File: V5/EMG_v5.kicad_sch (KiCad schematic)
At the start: 20 parts, among them J1 SJ1-3523N, J2 Output, U1 INA333xxDGK, U2 MCP6002-xP

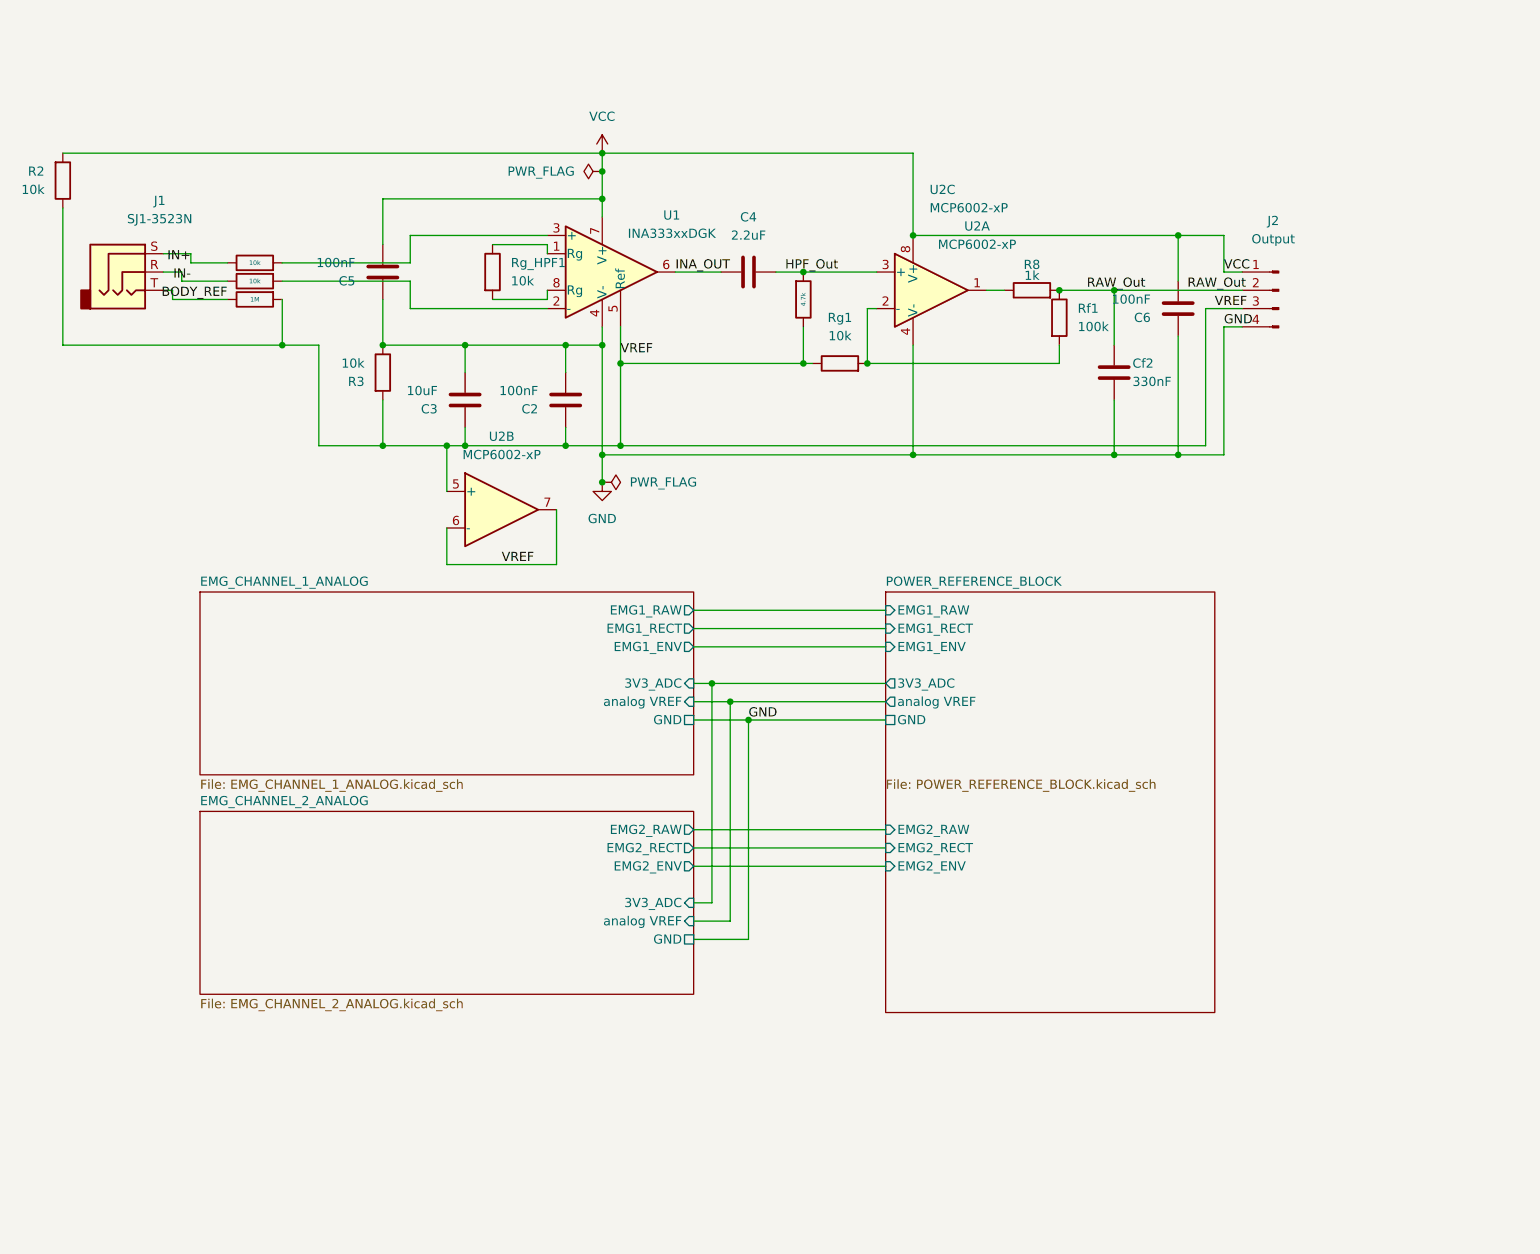
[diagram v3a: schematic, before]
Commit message: remove legacy root emg schematic block
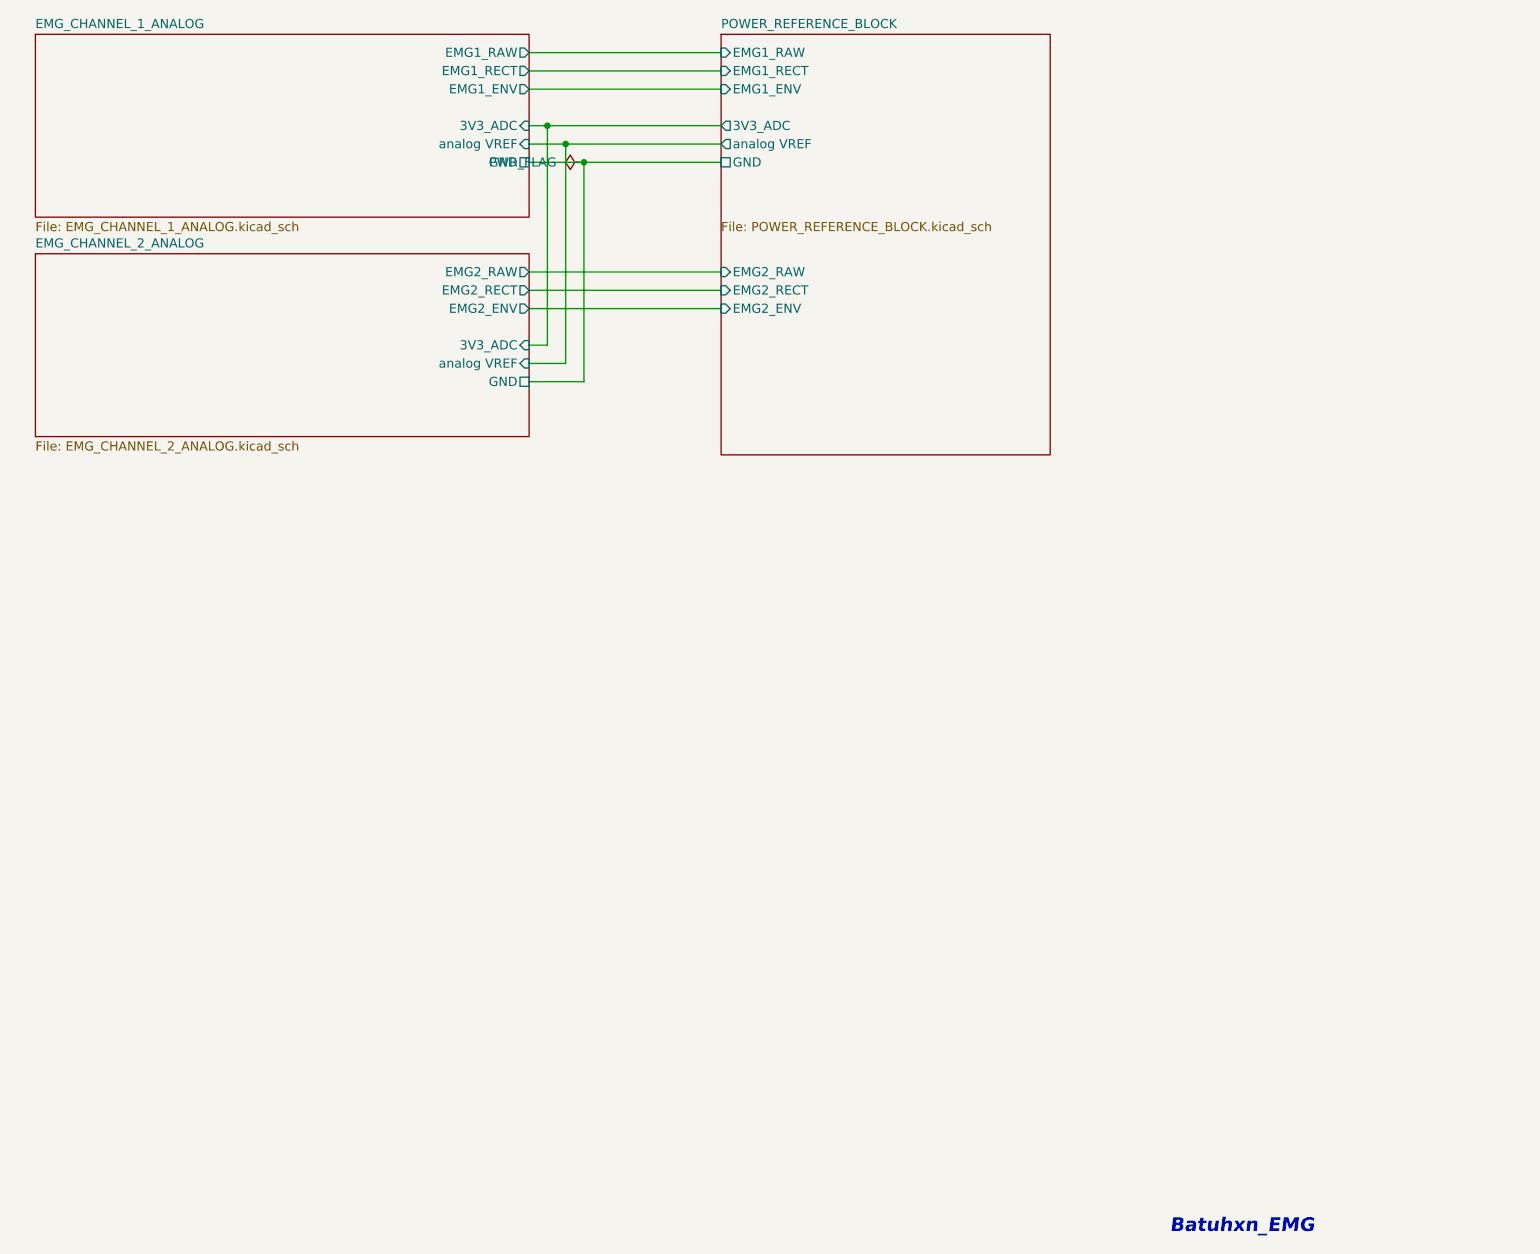
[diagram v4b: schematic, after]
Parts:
- removed C2, C5, C6: 100nF, Capacitor_THT:C_Disc_D5.0mm_W2.5mm_P5.00mm, symbol Device:C
- removed C3: 10uF, Capacitor_THT:CP_Radial_D5.0mm_P2.50mm, symbol Device:C
- removed C4: 2.2uF, Capacitor_THT:C_Disc_D5.0mm_W2.5mm_P5.00mm, symbol Device:C
- removed Cf2: 330nF, Capacitor_THT:C_Disc_D5.0mm_W2.5mm_P5.00mm, symbol Device:C
- removed J1: SJ1-3523N, Connector_Audio:Jack_3.5mm_CUI_SJ1-3523N_Horizontal, symbol Connector_Audio:AudioJack3
- removed J2: Output, Connector_PinHeader_2.54mm:PinHeader_1x04_P2.54mm_Vertical, symbol Connector:Conn_01x04_Pin
- removed R2, R3, R4, R5, Rg1, Rg_HPF1: 10k, Resistor_THT:R_Axial_DIN0207_L6.3mm_D2.5mm_P7.62mm_Horizontal, symbol Device:R
- removed R6: 4.7k, Resistor_THT:R_Axial_DIN0207_L6.3mm_D2.5mm_P7.62mm_Horizontal, symbol Device:R
- removed R7: 1M, Resistor_THT:R_Axial_DIN0207_L6.3mm_D2.5mm_P7.62mm_Horizontal, symbol Device:R
- removed R8: 1k, Resistor_THT:R_Axial_DIN0207_L6.3mm_D2.5mm_P7.62mm_Horizontal, symbol Device:R
- removed Rf1: 100k, Resistor_THT:R_Axial_DIN0207_L6.3mm_D2.5mm_P7.62mm_Horizontal, symbol Device:R
- removed U1: INA333xxDGK, Package_SO:VSSOP-8_3x3mm_P0.65mm, symbol Amplifier_Instrumentation:INA333xxDGK
- removed U2: MCP6002-xP, Package_DIP:DIP-8_W7.62mm, symbol Amplifier_Operational:MCP6002-xP
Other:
- note added: "Batuhxn_EMG"

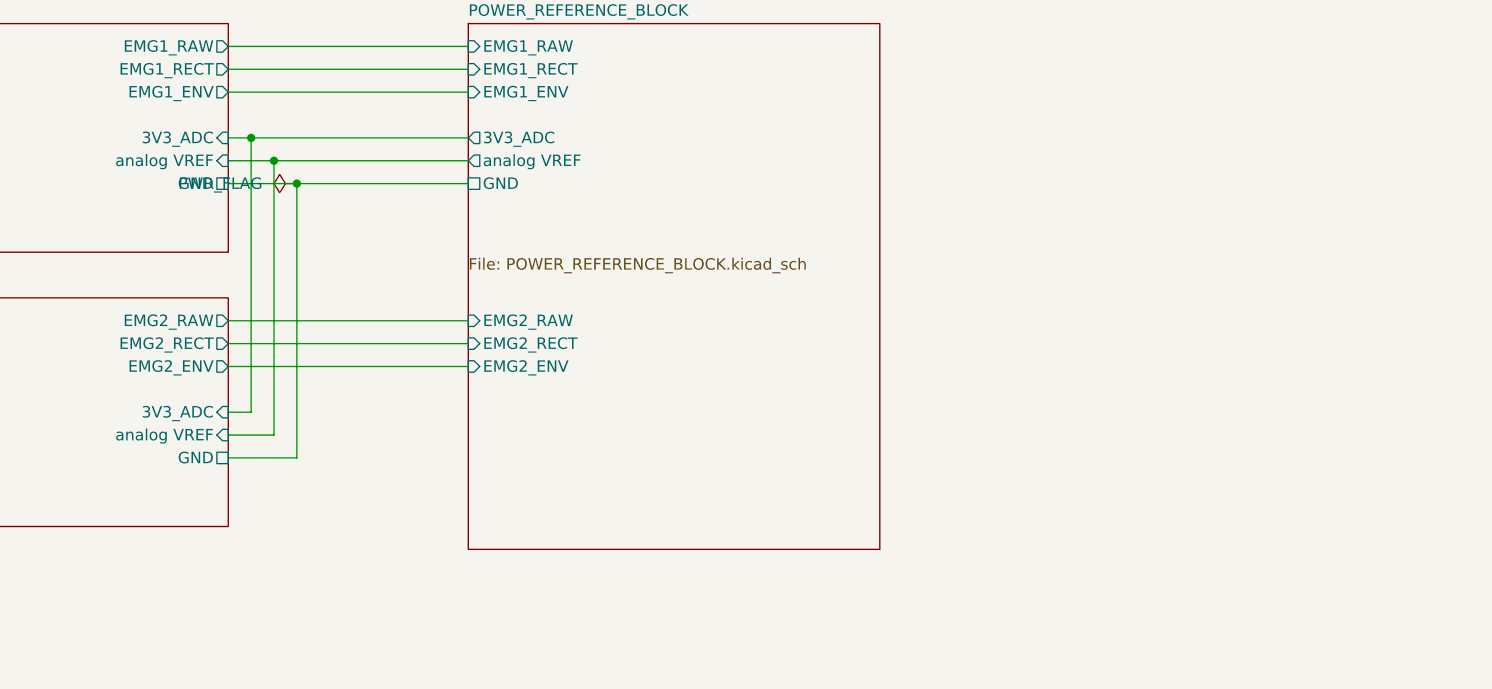
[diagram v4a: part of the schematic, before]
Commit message: connect dstk spi and mark unused pins
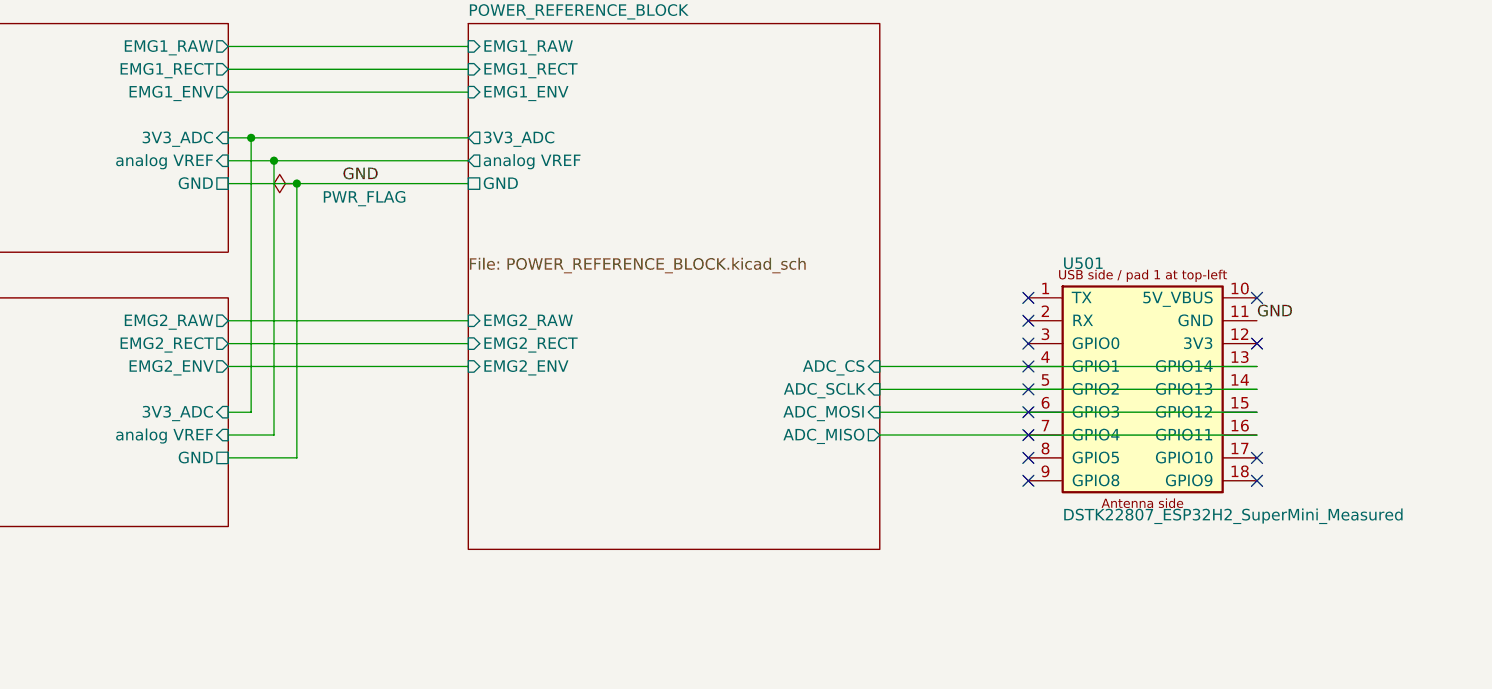
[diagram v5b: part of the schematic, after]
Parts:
- added U501: DSTK22807_ESP32H2_SuperMini_Measured, EMG_V5:DSTK22807_ESP32H2_SuperMini_Carrier_Measured_THT, symbol EMG_V5:DSTK22807_ESP32H2_SuperMini_Measured
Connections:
- new net GND: U501.11 (GND)
- new net POWER_REFERENCE_BLOCK/ADC_CS: U501.13 (GPIO14)
- new net POWER_REFERENCE_BLOCK/ADC_MISO: U501.16 (GPIO11)
- new net POWER_REFERENCE_BLOCK/ADC_MOSI: U501.15 (GPIO12)
- new net POWER_REFERENCE_BLOCK/ADC_SCLK: U501.14 (GPIO13)
- no-connect marks 0 -> 13
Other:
- sheet POWER_REFERENCE_BLOCK ports: added ADC_CS, ADC_MISO, ADC_MOSI, ADC_SCLK; removed none

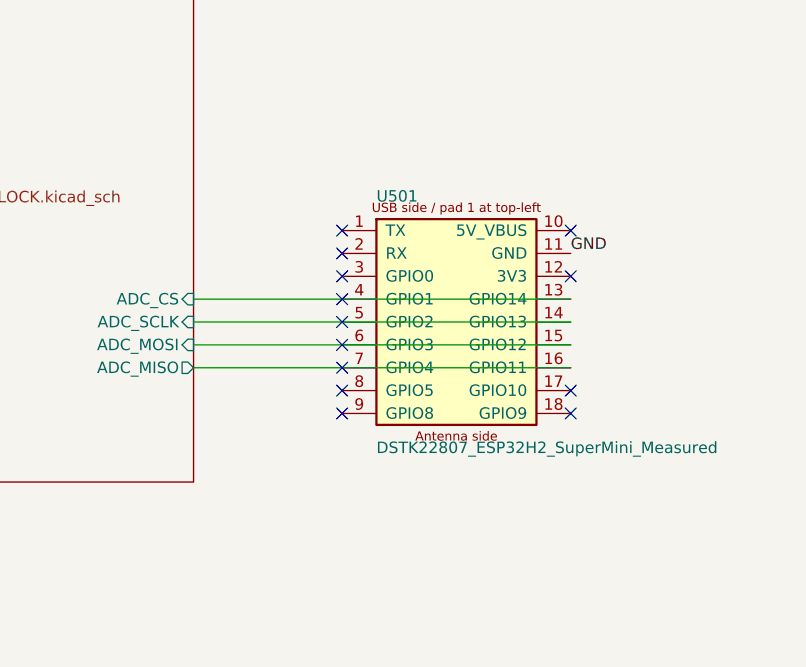
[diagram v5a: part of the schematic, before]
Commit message: refine root schematic layout
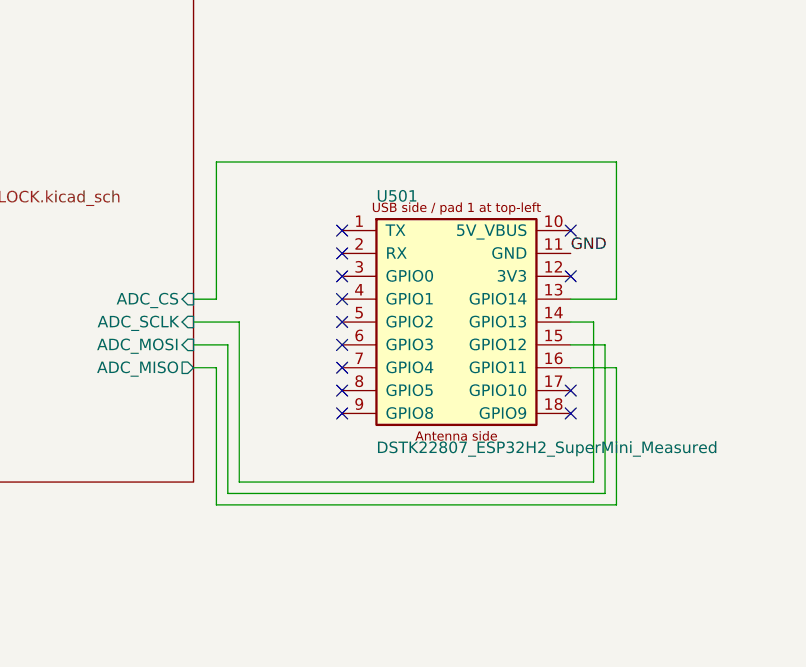
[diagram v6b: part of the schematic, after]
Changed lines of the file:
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@@
 		(color 0 0 0 0)
 	)
-	(wire
-		(pts
-			(xy 168.91 67.31) (xy 210.82 67.31)
+	(no_connect
+		(at 185.42 54.61)
+	)
+	(no_connect
+		(at 185.42 57.15)
+	)
+	(no_connect
+		(at 185.42 59.69)
+	)
+	(no_connect
+		(at 185.42 62.23)
+	)
+	(no_connect
+		(at 185.42 64.77)
+	)
+	(no_connect
+		(at 185.42 67.31)
+	)
+	(no_connect
+		(at 185.42 69.85)
+	)
+	(no_connect
+		(at 185.42 72.39)
+	)
+	(no_connect
+		(at 185.42 74.93)
+	)
+	(no_connect
+		(at 210.82 54.61)
+	)
+	(no_connect
+		(at 210.82 59.69)
+	)
+	(no_connect
+		(at 210.82 72.39)
+	)
+	(no_connect
+		(at 210.82 74.93)
+	)
+	(wire
+		(pts
+			(xy 215.9 46.99) (xy 171.45 46.99)
 		)
 		(stroke
@@
 	(wire
 		(pts
+			(xy 171.45 62.23) (xy 168.91 62.23)
+		)
+		(stroke
+			(width 0)
+			(type default)
+		)
+	)
+	(wire
+		(pts
+			(xy 172.72 67.31) (xy 168.91 67.31)
+		)
+		(stroke
+			(width 0)
+			(type default)
+		)
+	)
+	(wire
+		(pts
+			(xy 210.82 62.23) (xy 215.9 62.23)
+		)
+		(stroke
+			(width 0)
+			(type default)
+		)
+	)
+	(wire
+		(pts
+			(xy 215.9 69.85) (xy 215.9 85.09)
+		)
+		(stroke
+			(width 0)
+			(type default)
+		)
+	)
+	(wire
+		(pts
+			(xy 215.9 62.23) (xy 215.9 46.99)
+		)
+		(stroke
+			(width 0)
+			(type default)
+		)
+	)
+	(wire
+		(pts
+			(xy 172.72 83.82) (xy 172.72 67.31)
+		)
+		(stroke
+			(width 0)
+			(type default)
+		)
+	)
+	(wire
+		(pts
+			(xy 171.45 85.09) (xy 171.45 69.85)
+		)
+		(stroke
+			(width 0)
+			(type default)
+		)
+	)
+	(wire
+		(pts
+			(xy 215.9 85.09) (xy 171.45 85.09)
+		)
+		(stroke
+			(width 0)
+			(type default)
+		)
+	)
+	(wire
+		(pts
 			(xy 96.52 57.15) (xy 123.19 57.15)
 		)
@@
 	(wire
 		(pts
+			(xy 173.99 82.55) (xy 173.99 64.77)
+		)
+		(stroke
+			(width 0)
+			(type default)
+		)
+	)
+	(wire
+		(pts
 			(xy 96.52 26.67) (xy 123.19 26.67)
 		)
@@
 	(wire
 		(pts
+			(xy 213.36 82.55) (xy 173.99 82.55)
+		)
+		(stroke
+			(width 0)
+			(type default)
+		)
+	)
+	(wire
+		(pts
+			(xy 171.45 69.85) (xy 168.91 69.85)
+		)
+		(stroke
+			(width 0)
+			(type default)
+		)
+	)
+	(wire
+		(pts
 			(xy 96.52 67.31) (xy 99.06 67.31)
 		)
@@
 	(wire
 		(pts
-			(xy 168.91 62.23) (xy 210.82 62.23)
-		)
-		(stroke
-			(width 0)
-			(type default)
-		)
-	)
-	(wire
-		(pts
-			(xy 168.91 69.85) (xy 210.82 69.85)
+			(xy 210.82 69.85) (xy 215.9 69.85)
+		)
+		(stroke
+			(width 0)
+			(type default)
+		)
+	)
+	(wire
+		(pts
+			(xy 173.99 64.77) (xy 168.91 64.77)
+		)
+		(stroke
+			(width 0)
+			(type default)
+		)
+	)
+	(wire
+		(pts
+			(xy 210.82 64.77) (xy 213.36 64.77)
+		)
+		(stroke
+			(width 0)
+			(type default)
+		)
+	)
+	(wire
+		(pts
+			(xy 210.82 67.31) (xy 214.63 67.31)
+		)
+		(stroke
+			(width 0)
+			(type default)
+		)
+	)
+	(wire
+		(pts
+			(xy 214.63 67.31) (xy 214.63 83.82)
+		)
+		(stroke
+			(width 0)
+			(type default)
+		)
+	)
+	(wire
+		(pts
+			(xy 214.63 83.82) (xy 172.72 83.82)
+		)
+		(stroke
+			(width 0)
+			(type default)
+		)
+	)
+	(wire
+		(pts
+			(xy 213.36 64.77) (xy 213.36 82.55)
 		)
 		(stroke
@@
 	(wire
 		(pts
-			(xy 168.91 64.77) (xy 210.82 64.77)
+			(xy 171.45 46.99) (xy 171.45 62.23)
 		)
 		(stroke
@@
 		)
 	)
-	(no_connect
-		(at 185.42 54.61)
-	)
-	(no_connect
-		(at 185.42 57.15)
-	)
-	(no_connect
-		(at 185.42 59.69)
-	)
-	(no_connect
-		(at 185.42 62.23)
-	)
-	(no_connect
-		(at 185.42 64.77)
-	)
-	(no_connect
-		(at 185.42 67.31)
-	)
-	(no_connect
-		(at 185.42 69.85)
-	)
-	(no_connect
-		(at 185.42 72.39)
-	)
-	(no_connect
-		(at 185.42 74.93)
-	)
-	(no_connect
-		(at 210.82 54.61)
-	)
-	(no_connect
-		(at 210.82 59.69)
-	)
-	(no_connect
-		(at 210.82 72.39)
-	)
-	(no_connect
-		(at 210.82 74.93)
-	)
 	(symbol

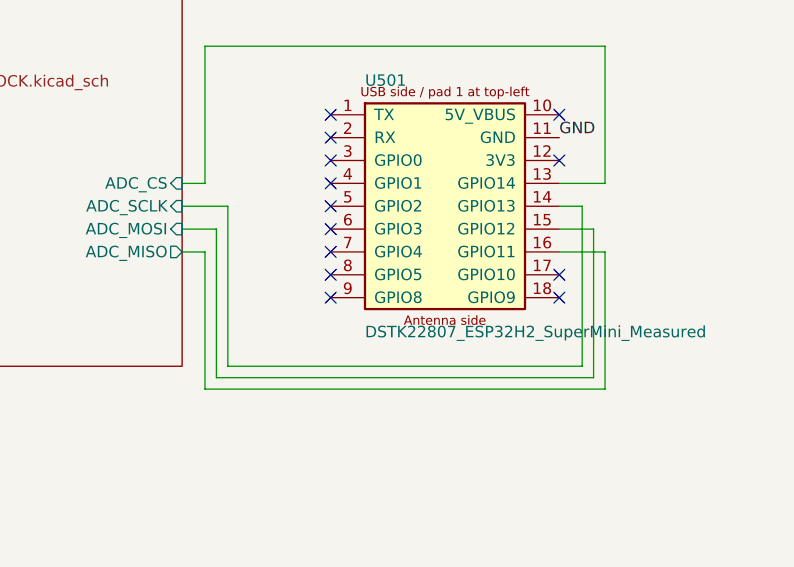
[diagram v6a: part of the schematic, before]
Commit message: remap adc sclk to gpio4
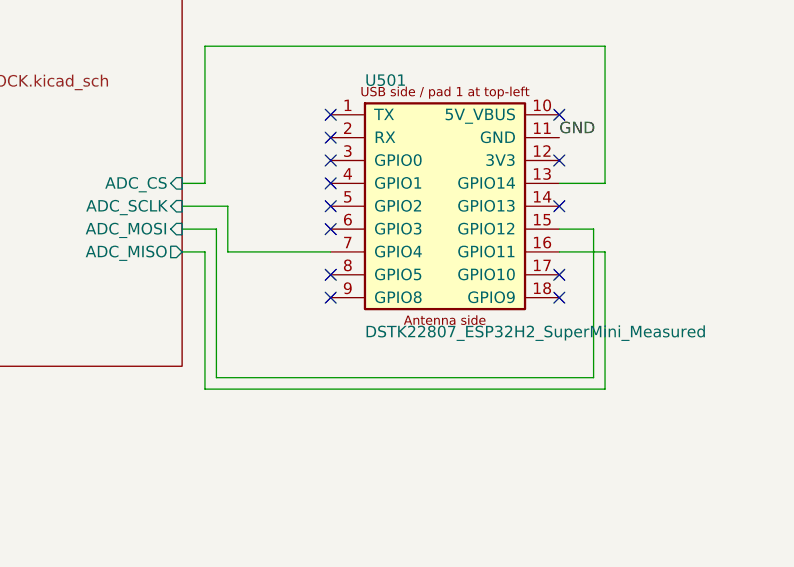
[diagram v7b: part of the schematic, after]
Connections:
- net POWER_REFERENCE_BLOCK/ADC_SCLK: now also U501.7 (GPIO4); no longer U501.14 (GPIO13)
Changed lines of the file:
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@@
 	)
 	(no_connect
-		(at 185.42 69.85)
+		(at 210.82 64.77)
 	)
 	(no_connect
@@
 	(wire
 		(pts
-			(xy 173.99 82.55) (xy 173.99 64.77)
+			(xy 173.99 69.85) (xy 173.99 64.77)
 		)
 		(stroke
@@
 	(wire
 		(pts
-			(xy 213.36 82.55) (xy 173.99 82.55)
+			(xy 185.42 69.85) (xy 173.99 69.85)
 		)
 		(stroke
@@
 	(wire
 		(pts
-			(xy 210.82 64.77) (xy 213.36 64.77)
-		)
-		(stroke
-			(width 0)
-			(type default)
-		)
-	)
-	(wire
-		(pts
 			(xy 210.82 67.31) (xy 214.63 67.31)
 		)
@@
 		)
 		(stroke
-			(width 0)
-			(type default)
-		)
-	)
-	(wire
-		(pts
-			(xy 213.36 64.77) (xy 213.36 82.55)
-		)
-		(stroke
